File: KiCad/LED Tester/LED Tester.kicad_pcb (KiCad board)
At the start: 2 copper layers, 117 x 62 mm, 49 parts, among them J1 2V_5mA, J10 3V_10mA, J11 3V_15mA, J12 3V_20mA, J2 2V_10mA, J3 2V_15mA, J4 2V_20mA, J5 2.5V_5mA, J6 2.5V_10mA, J7 2.5V_15mA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

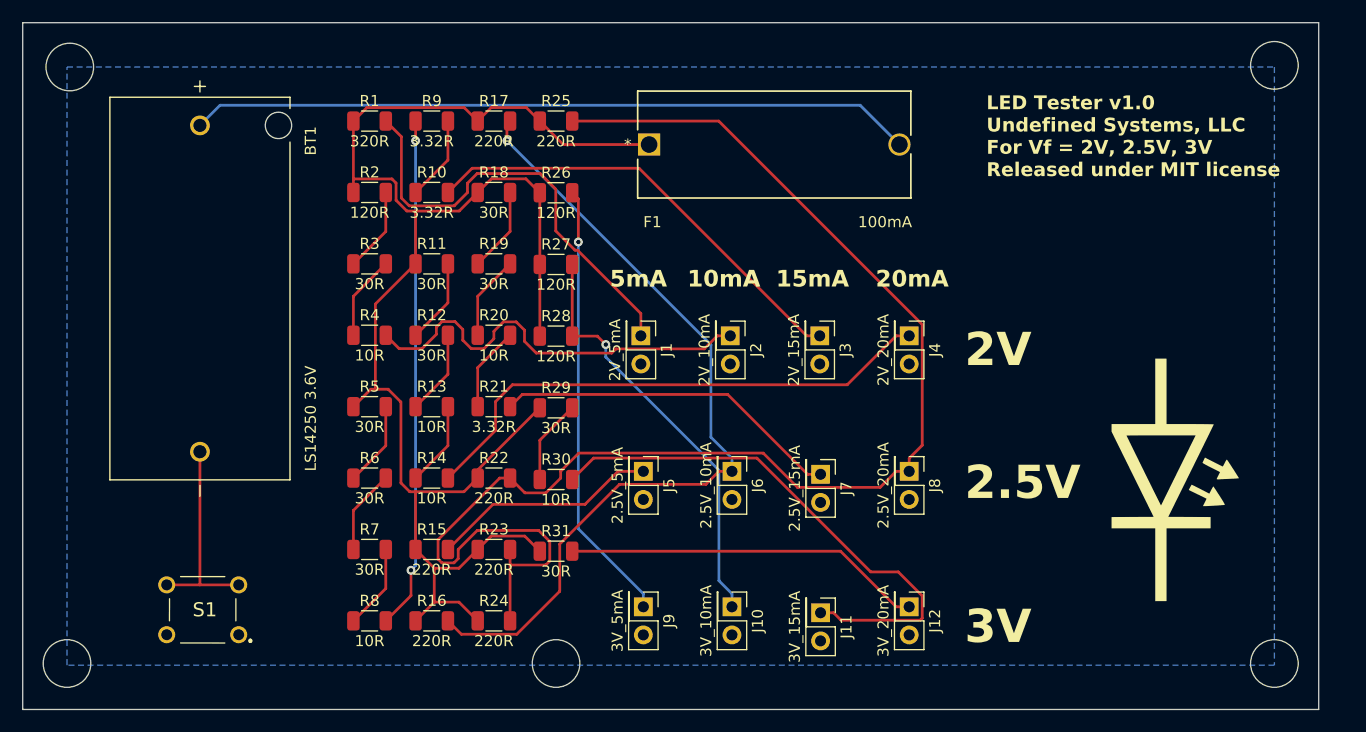
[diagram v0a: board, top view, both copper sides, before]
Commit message: update pcb size
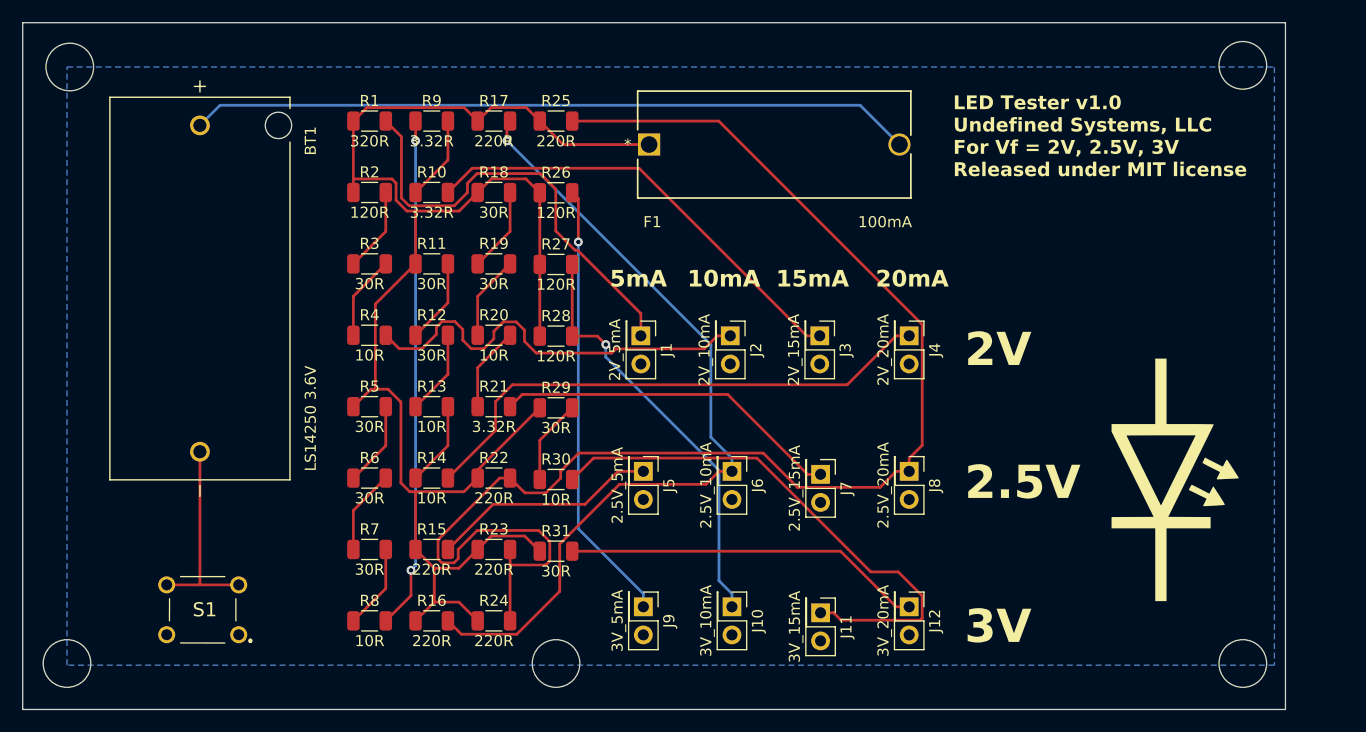
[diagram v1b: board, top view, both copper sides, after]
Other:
- board size 117 x 62 mm -> 114 x 62 mm
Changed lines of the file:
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@@
   (gr_circle (center 121.15 114.85) (end 123.3 114.85)
     (stroke (width 0.1) (type default)) (fill none) (layer "Edge.Cuts"))
-  (gr_circle (center 186 114.85) (end 188.15 114.85)
+  (gr_circle (center 183.15 114.85) (end 185.3 114.85)
     (stroke (width 0.1) (type default)) (fill none) (layer "Edge.Cuts"))
-  (gr_rect (start 73 57) (end 190 119)
+  (gr_rect (start 73 57) (end 187 119)
     (stroke (width 0.1) (type default)) (fill none) (layer "Edge.Cuts"))
-  (gr_circle (center 186 60.85) (end 188.15 60.85)
+  (gr_circle (center 183.15 60.85) (end 185.3 60.85)
     (stroke (width 0.1) (type default)) (fill none) (layer "Edge.Cuts"))
   (gr_circle (center 77 114.85) (end 79.15 114.85)
@@
     (effects (font (size 3 3) (thickness 0.2) bold) (justify left bottom))
   )
-  (gr_text "LED Tester v1.0\nUndefined Systems, LLC\nFor Vf = 2V, 2.5V, 3V\nReleased under MIT license" (at 160 71) (layer "F.SilkS")
+  (gr_text "LED Tester v1.0\nUndefined Systems, LLC\nFor Vf = 2V, 2.5V, 3V\nReleased under MIT license" (at 157 71) (layer "F.SilkS")
     (effects (font (size 1.25 1.25) (thickness 0.2) bold) (justify left bottom))
   )
